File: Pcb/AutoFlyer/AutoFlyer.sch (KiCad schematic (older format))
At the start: 19 parts, among them J1 Screw_Terminal_1x02, J2 Programmer, J3 Battery, SW1 SW_Push, U1 ATTINY45-20PU, U2 LD1117S33TR_SOT223, U3 H-Bridge-DMHC3025LSD, X1 HOLE, X2 HOLE

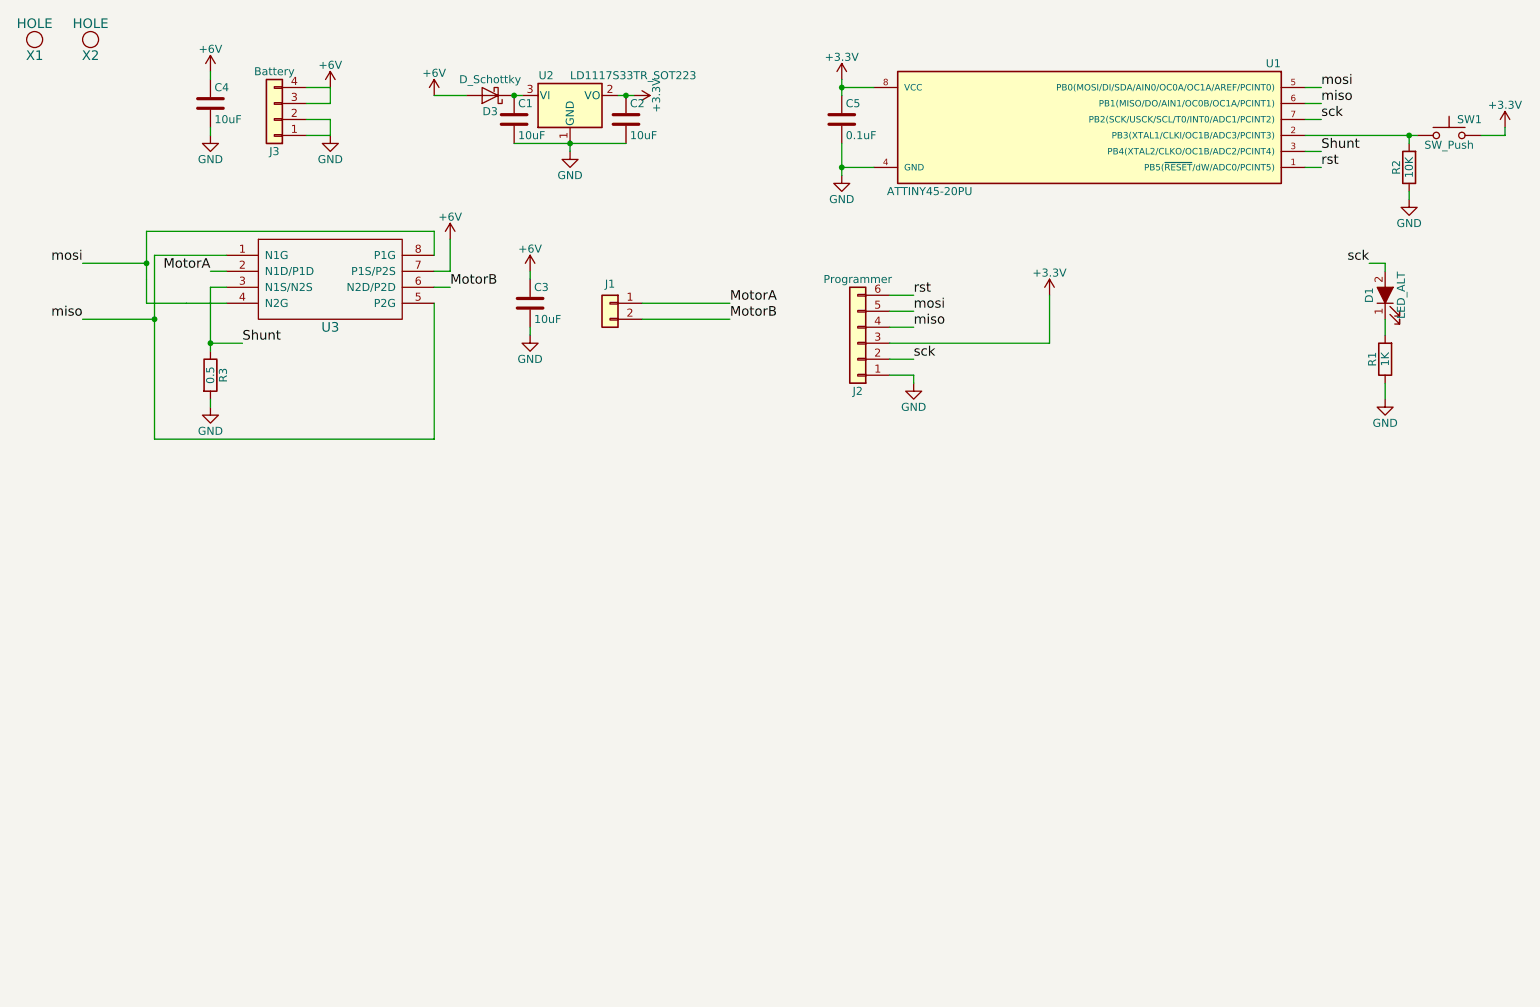
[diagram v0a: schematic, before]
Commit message: Add autoflyer pcb
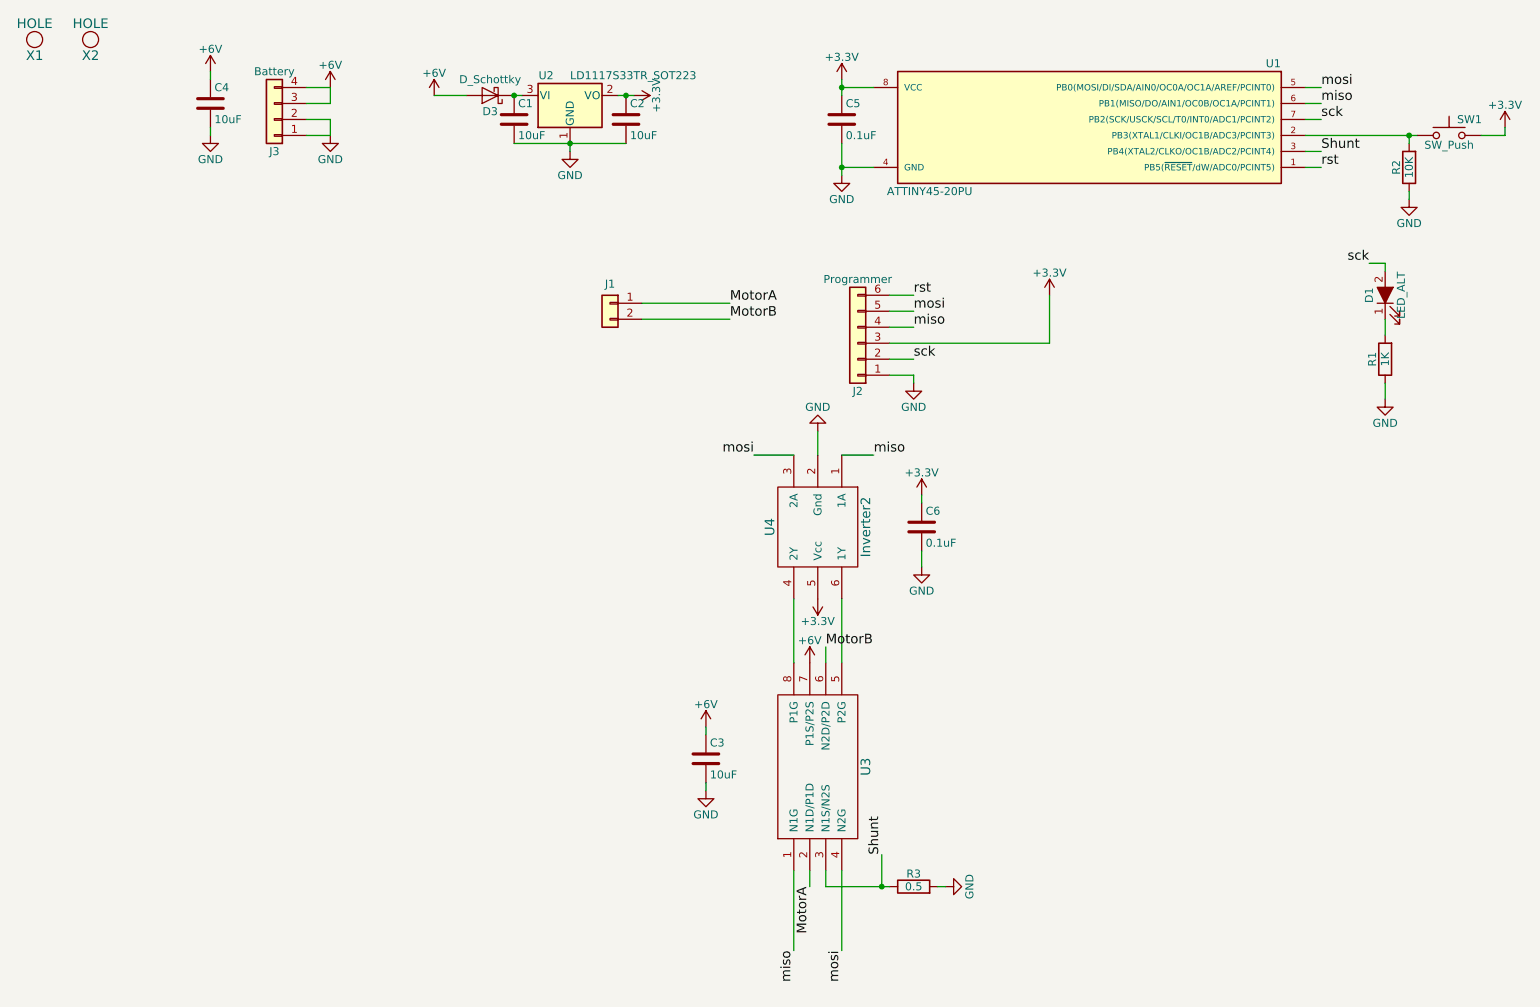
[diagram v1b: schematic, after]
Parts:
- added C6: 0.1uF, Capacitors_SMD:C_0603, symbol C
- added U4: Inverter2, TO_SOT_Packages_SMD:SOT-363_SC-70-6, symbol Inverter2
- D1: footprint LEDs:LED_0603 -> LEDs:LED_0805
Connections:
- net +3V3: now also C6.1, U4.5 (Vcc)
- net GND: now also C6.2, U4.2 (Gnd)
- net miso: now also U4.1 (1A); no longer U3.5 (P2G)
- net mosi: now also U4.3 (2A); no longer U3.8 (P1G)
- new net: U3.5 (P2G), U4.6 (1Y)
- new net: U3.8 (P1G), U4.4 (2Y)
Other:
- moved on the sheet: C3, R3, U3

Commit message: Update auto flyer and some documentation
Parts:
- removed C4: 10uF, Capacitors_SMD:C_1206, symbol C
- removed C6: 0.1uF, Capacitors_SMD:C_0603, symbol C
- removed U1: ATTINY45-20PU, SMD_Packages:SOIC-8-N, symbol ATTINY45-20PU
- removed U4: Inverter2, TO_SOT_Packages_SMD:SOT-363_SC-70-6, symbol Inverter2
- added U1: ATTINY44-20SSU, Housings_SOIC:SOIC-14_3.9x8.7mm_Pitch1.27mm, symbol atmel:ATTINY44-20SSU
- C1, C2, C3, C5: symbol C -> Device:C
- D1: symbol LED_ALT -> Device:LED_ALT
- D3: symbol D_Schottky -> Device:D_Schottky
- J1: symbol Conn_01x02 -> conn:Conn_01x02
- J2: symbol Conn_01x06 -> conn:Conn_01x06
- J3: symbol Conn_01x04 -> conn:Conn_01x04
- R1, R2, R3: symbol R -> Device:R
- SW1: symbol SW_Push -> switches:SW_Push
- U2: symbol LD1117S33TR_SOT223 -> regul:LD1117S33TR_SOT223
- U3: symbol H-Bridge-DMHC3025LSD -> eew:H-Bridge-DMHC3025LSD
- X1, X2: symbol HOLE -> CA6:HOLE
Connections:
- net +3V3: now also U1.1 (VCC)
- net +6V: no longer J3.3 (Pin_3)
- net GND: now also U1.14 (GND); no longer J3.2 (Pin_2)
- net miso: now also U1.8 ((PCINT5/DO/MISO/OC1B/ADC5)PA5); no longer U3.1 (N1G)
- net mosi: now also U1.7 ((PCINT6/SDA/DI/MOSI/OC1A/ADC6)PA6); no longer U3.4 (N2G)
- net rst: now also U1.4 ((PCINT11/dW/~RESET~)PB3)
- net sck: now also U1.9 ((PCINT4/USCK/SCL/T1/ADC4)PA4); no longer D1.2 (A)
- net c2: now reaches U3.5 (P2G)
- net c2: now also U1.3 ((PCINT9/XTAL2)PB1)
- net c3: now reaches U3.8 (P1G)
- net c3: now also U1.2 ((PCINT8/CLKI/XTAL1)PB0)
- net at R2.2, SW1.1: now also U1.12 ((PCINT1/AIN0/ADC1)PA1)
- net Shunt renamed shunt
- net shunt: now also U1.13 ((PCINT0/AREF/ADC0)PA0)
- new net: J3.2 (Pin_2), J3.3 (Pin_3)
- new net c0: U1.6 ((PCINT7/ICP/OC0B/ADC7)PA7), U3.1 (N1G)
- new net c1: U1.5 ((PCINT10/CKOUT/OC0A/INT0)PB2), U3.4 (N2G)
- new net led: D1.2 (A), U1.11 ((PCINT2/AIN1/ADC2)PA2)
- no-connect marks 0 -> 1
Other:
- moved on the sheet: C3, C5, D1, J1, J2, R1, R2, R3, SW1, U3
